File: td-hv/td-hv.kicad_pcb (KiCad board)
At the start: 2 copper layers, 100 x 60 mm, 39 parts, among them J1 Conn_01x06_Male, Q1 IMBF170R450M1XTMA1, U1 UCC2801, U2 TL081, U3 LM2903

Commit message: some td-hv layout
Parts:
- added C10: 0.1uF, Capacitor_SMD:C_0805_2012Metric, F.Cu at (-69.0, -17.0)
- added D4: BAS21, Package_TO_SOT_SMD:SOT-23, F.Cu at (-15.3, -29.9)
- added D5: SMAJ400ALFCT-ND, Diode_SMD:D_SMA, F.Cu at (-15.5, -24.5)
- added R14: 50, Resistor_SMD:R_1206_3216Metric, F.Cu at (-22.9, -30.4)
- J1: value Conn_01x06_Male -> Conn_01x07_Male; footprint Connector_JST:JST_XH_B6B-XH-AM_1x06_P2.50mm_Vertical -> Connector_JST:JST_XH_B7B-XH-AM_1x07_P2.50mm_Vertical
- R10, R4: footprint Resistor_SMD:R_0805_2012Metric -> Resistor_SMD:R_1206_3216Metric
- R11: value 100k -> 120
- R12: value 100 -> 50
- U2: value TL081 -> TLC272
- moved C4 60.3 mm to (-8.00, -15.0)
- moved C5 54.2 mm to (-7.05, -24.0), turned to 0 degrees
- moved R10 46.7 mm to (-23.0, -24.5), turned to 0 degrees
- moved C8 43.3 mm to (-61.0, -31.5), turned to 0 degrees
- moved R11 38.5 mm to (-77.0, -17.0)
- moved Q1 36.0 mm to (-45.0, -27.5)
- moved R4 35.8 mm to (-56.0, -24.0), turned to 270 degrees
- moved D1 35.5 mm to (-59.0, -12.5)
- moved R5 35.5 mm to (-59.0, -15.5)
- moved R3 35.2 mm to (-56.0, -31.0), turned to 180 degrees
- moved C7 34.7 mm to (-30.9, -24.5), turned to 0 degrees
- moved C6 34.5 mm to (-63.0, -11.5), turned to 270 degrees
- moved E1 33.3 mm to (-31.4, -31.0)
- moved R12 31.3 mm to (-73.0, -17.0), turned to 0 degrees
- moved C1 30.1 mm to (-71.0, -25.4)
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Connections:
- net Net-(C7-Pad2) renamed /snubber_node
- net Net-(F1-Pad2) renamed /vbus_in
- C3 pad 2: GND -> Net-(C3-Pad2)
- C8 pad 1: +12V -> Net-(C8-Pad1)
- R11 pad 1: Net-(L1-Pad7) -> Net-(C3-Pad2)
- R11 pad 2: GND -> /sync_in
- R12 pad 1: /eht_current -> Net-(C3-Pad2)
- R13 pad 2: Net-(R13-Pad2) -> Net-(C8-Pad1)
- R2 pad 2: GND -> /ucc3801_ref
- U1 pad 7: Net-(R13-Pad2) -> Net-(C8-Pad1)
- U2 pad 1: Net-(U2-Pad1) -> /eht_voltage
- U2 pad 5: Net-(U2-Pad5) -> (no net)
- U2 pad 6: /eht_voltage -> (no net)
- U2 pad 7: +12V -> (no net)
- U2 pad 8: Net-(U2-Pad8) -> +12V
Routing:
- net Net-(L1-Pad7): track 0.00 -> 57.2 mm
- net /eht_current: track 0.00 -> 54.5 mm, vias 0 -> 1
- net /fb: track 0.00 -> 53.4 mm
- net /eht_voltage: track 0.00 -> 49.0 mm, vias 0 -> 2
- net /sw: track 0.00 -> 33.2 mm
- net Net-(RV1-Pad2): track 0.00 -> 26.2 mm
- net VBUS: track 0.00 -> 24.8 mm
- net /sync_in: track 0.00 -> 24.6 mm
- net +12V: track 0.00 -> 24.2 mm, vias 0 -> 1
- net /cs: track 0.00 -> 22.5 mm
- net /~xray_protect: track 0.00 -> 16.8 mm, vias 0 -> 2
- net Net-(C6-Pad1): track 0.00 -> 16.3 mm
- net /ucc3801_ref: track 0.00 -> 13.6 mm, vias 0 -> 2
- net /vbus_in: track 0.00 -> 13.4 mm
- net Net-(D1-Pad1): track 0.00 -> 12.8 mm
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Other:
- board size 100 x 60 mm -> 90 x 66 mm
- net class hv added: clearance 1.5, trace_width 0.25, via_dia 0.8, via_drill 0.4
- board text added: "+12v"
- board text added: "b+"
- board text added: "eht_i"
- board text added: "eht_v"
- board text added: "gnd"
- board text added: "sync"
- board text added: "xray"
- board text removed: "Discharge Capacitors Before Servicing"

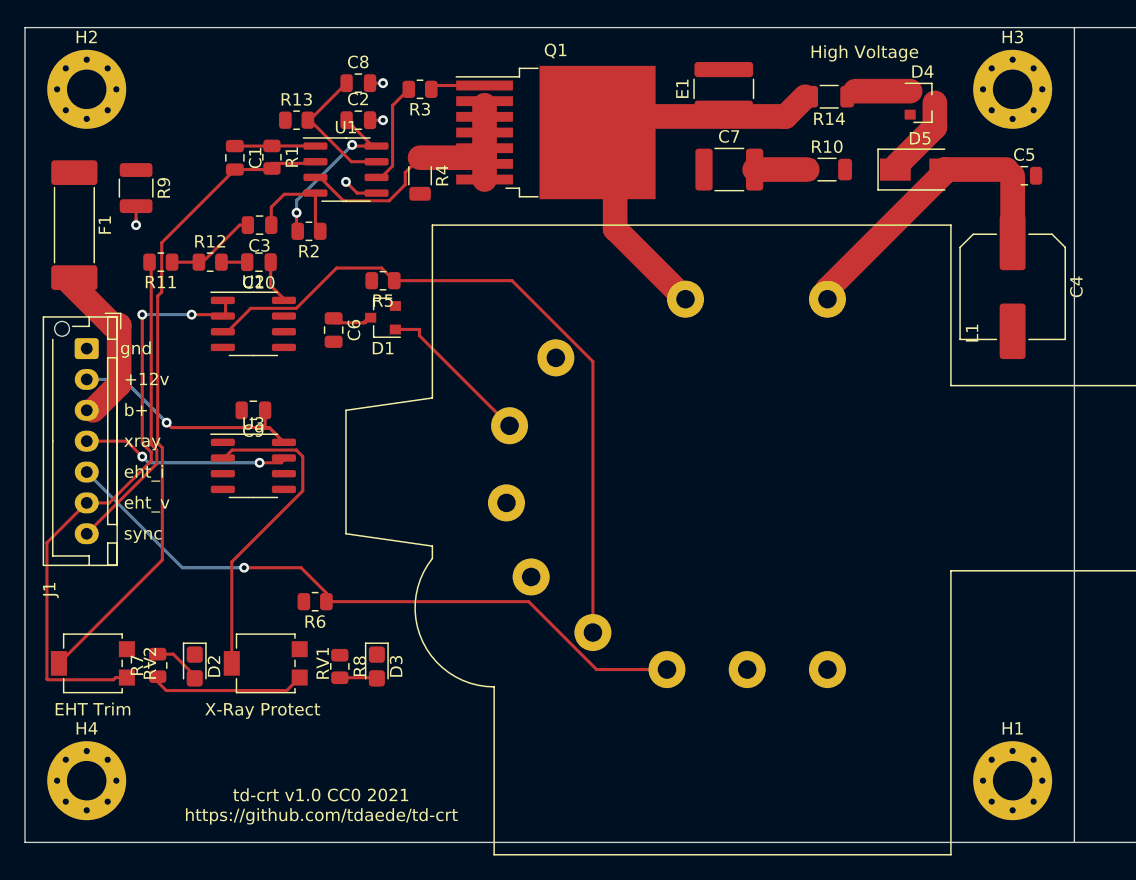
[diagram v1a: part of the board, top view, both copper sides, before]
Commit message: add output for vertical ssr
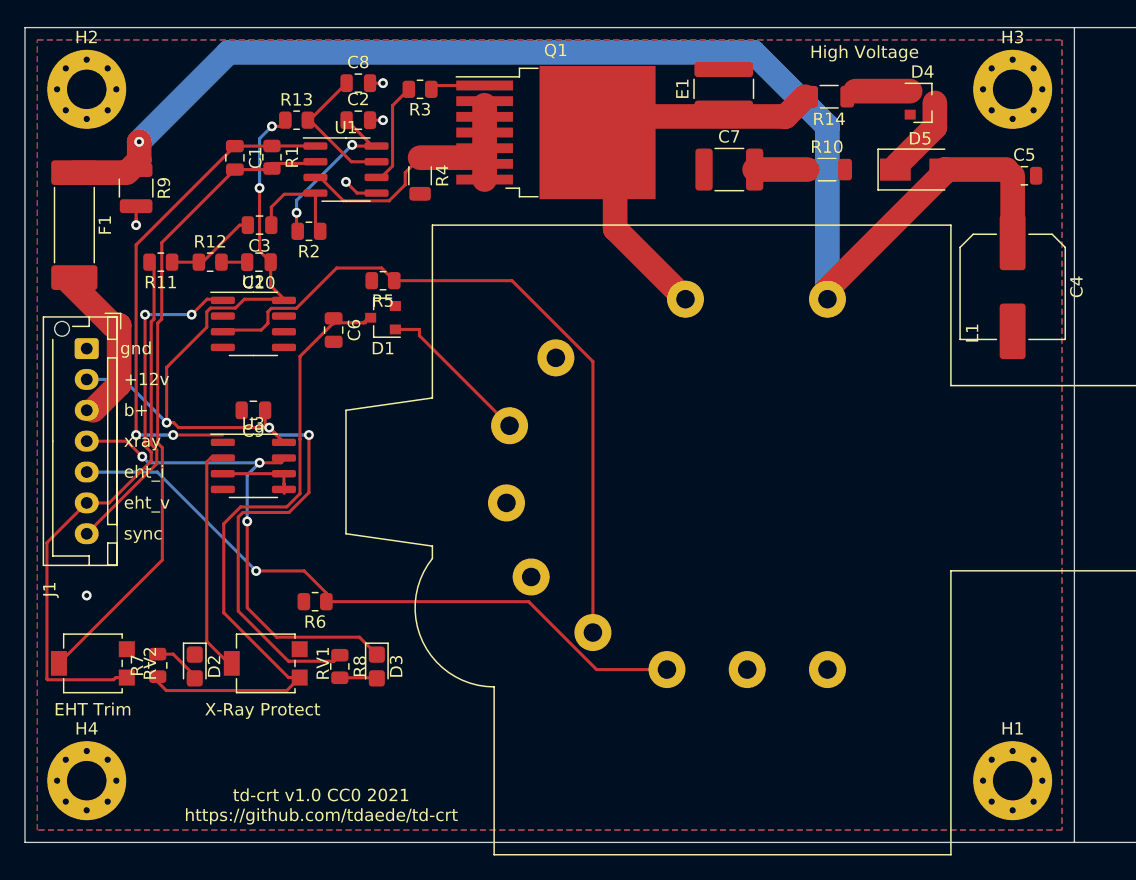
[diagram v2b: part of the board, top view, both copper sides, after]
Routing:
- net VBUS: track 24.8 -> 107.0 mm, vias 0 -> 1
- net +12V: track 24.2 -> 86.4 mm, vias 1 -> 5
- net Net-(C6-Pad1): track 16.3 -> 53.9 mm
- net /comp: track 5.49 -> 39.2 mm, vias 0 -> 2
- net /~xray_protect: track 16.8 -> 41.1 mm, vias 2 -> 3
- net Net-(RV1-Pad2): track 26.2 -> 18.7 mm
- net /ucc3801_ref: track 13.6 -> 20.3 mm
- net /eht_voltage: track 49.0 -> 47.9 mm
- net Net-(L1-Pad7): track 57.2 -> 57.7 mm
- net (no net): vias 0 -> 1
- added copper zone on B.Cu, net GND
- added copper zone on F.Cu, net GND

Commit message: stuff
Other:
- board size 90 x 66 mm -> 85 x 66 mm

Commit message: more td-hv layout
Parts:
- added REF**: KiCad-Logo_5mm_SilkScreen, Symbol:KiCad-Logo_5mm_SilkScreen, F.Cu at (-75.8, -33.2)
- added REF**: OSHW-Symbol_6.7x6mm_SilkScreen, Symbol:OSHW-Symbol_6.7x6mm_SilkScreen, F.Cu at (-7.80, 13.2)
- moved R5 17.8 mm to (-73.4, -5.00), turned to 0 degrees
- moved H2 7.07 mm to (-88.0, -36.0)
- moved H3 5.00 mm to (-8.00, -36.0)
- moved H4 5.00 mm to (-88.0, 25.0)
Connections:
- J1 pad 6: /eht_voltage -> /fb
- R5 pad 1: Net-(L1-Pad7) -> Net-(R5-Pad1)
- RV2 pad 1: /eht_voltage -> Net-(L1-Pad7)
- RV2 pad 2: /fb -> Net-(R5-Pad1)
- RV2 pad 3: GND -> Net-(R5-Pad1)
- U2 pad 1: /eht_voltage -> /fb
- U2 pad 2: /eht_voltage -> /fb
- U2 pad 3: Net-(L1-Pad7) -> Net-(R5-Pad1)
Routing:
- net /eht_voltage: track 47.9 -> 0.00 mm, vias 2 -> 0
- net Net-(R5-Pad1): track 0.00 -> 37.0 mm
- net /ucc3801_ref: track 20.3 -> 40.7 mm
- net /sw: track 33.2 -> 20.4 mm, vias 0 -> 13
- net Net-(L1-Pad7): track 57.7 -> 45.7 mm
- net VBUS: track 107.0 -> 115.4 mm
- net +12V: track 86.4 -> 79.8 mm
- net /fb: track 53.4 -> 54.5 mm
- net /sync_in: track 24.8 -> 24.1 mm
- net GND: vias 4 -> 41
- net (no net): vias 1 -> 0
- added copper zone on B.Cu, net /sw
- added copper zone on F.Cu, net /sw
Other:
- board size 85 x 66 mm -> 90 x 71 mm
- board text added: "td-hv v1.0 CERN OHL-W 2021 https://github.com/tdaede/td-crt"
- board text removed: "td-crt v1.0 CC0 2021 https://github.com/tdaede/td-crt"

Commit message: finish layout
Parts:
- removed REF**: KiCad-Logo_5mm_SilkScreen, Symbol:KiCad-Logo_5mm_SilkScreen
- removed REF**: OSHW-Symbol_6.7x6mm_SilkScreen, Symbol:OSHW-Symbol_6.7x6mm_SilkScreen
- added C11: 0.1uF, Capacitor_SMD:C_0805_2012Metric, F.Cu at (-65.5, -7.50)
- added C12: 0.001uF, Capacitor_SMD:C_0805_2012Metric, F.Cu at (-63.5, -12.5)
- added C13: 0.001uF, Capacitor_SMD:C_0805_2012Metric, F.Cu at (-47.5, -28.7)
- added C14: 0.1uF, Capacitor_SMD:C_0805_2012Metric, F.Cu at (-69.5, -7.50)
- added R16: 10k, Resistor_SMD:R_0805_2012Metric, F.Cu at (-58.9, -12.0)
- added R17: 10k, Resistor_SMD:R_0805_2012Metric, F.Cu at (-47.4, -31.5)
- added R18: 10, Resistor_SMD:R_0805_2012Metric, F.Cu at (-47.5, -34.0)
- added R19: 100k, Resistor_SMD:R_0805_2012Metric, F.Cu at (-69.5, -5.00)
- added R20: 100k, Resistor_SMD:R_0805_2012Metric, F.Cu at (-73.5, -7.50)
- added R21: 10k, Resistor_SMD:R_0805_2012Metric, F.Cu at (-76.9, -36.0)
- added R22: 100k, Resistor_SMD:R_0805_2012Metric, F.Cu at (-76.9, -32.5)
- C1: value 10000pF -> 0.1uF
- C3: value 22000pF -> 0.1uF
- C5: footprint Capacitor_SMD:C_0805_2012Metric -> Capacitor_SMD:C_1206_3216Metric
- C7: value 470pF 2000V NP0 -> 47pF 2000V NP0; footprint Capacitor_SMD:C_1812_4532Metric -> Capacitor_SMD:C_1206_3216Metric
- D2: value LED -> GREEN
- D3: value LED -> RED
- D4: value BAS21 -> GREEN; footprint Package_TO_SOT_SMD:SOT-23 -> LED_SMD:LED_0805_2012Metric
- D5: value SMAJ400ALFCT-ND -> GREEN; footprint Diode_SMD:D_SMA -> LED_SMD:LED_0805_2012Metric
- R10: value 20k -> 3k; footprint Resistor_SMD:R_1206_3216Metric -> Resistor_SMD:R_2512_6332Metric
- R11: value 120 -> 39k
- R12: value 50 -> 10k
- R13: value 1k -> 1.4k
- R14: value 50 -> 10k; footprint Resistor_SMD:R_1206_3216Metric -> Resistor_SMD:R_0805_2012Metric
- R2: value 10k -> 100k
- R3: value 1 -> 1M
- R4: value 1 -> 4.7
- U1: value UCC2801 -> UCC35701; footprint Package_SO:SOIC-8_3.9x4.9mm_P1.27mm -> Package_SO:SOIC-14_3.9x8.7mm_P1.27mm
- moved D5 57.6 mm to (-72.5, -32.5), turned to 180 degrees
- moved D4 57.5 mm to (-72.5, -36.0), turned to 180 degrees
- moved R14 45.5 mm to (-63.5, -10.0), turned to 0 degrees
- moved C5 34.6 mm to (-40.0, -34.5)
- moved C4 34.2 mm to (-40.0, -27.0)
- moved R4 23.5 mm to (-32.5, -22.0), turned to 180 degrees
- moved R10 21.1 mm to (-39.2, -38.0)
- moved R13 20.2 mm to (-47.5, -36.5), turned to 180 degrees
- moved Q1 18.8 mm to (-26.3, -29.5)
- moved E1 18.7 mm to (-13.5, -25.8), turned to 0 degrees
- moved C2 14.5 mm to (-47.5, -23.2)
- moved C7 13.1 mm to (-32.2, -37.5)
- moved C1 11.0 mm to (-60.0, -25.7), turned to 180 degrees
- moved U1 10.0 mm to (-53.8, -30.2), turned to 180 degrees
- moved R3 10.00 mm to (-47.5, -25.7), turned to 0 degrees
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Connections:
- net /~xray_protect renamed /~{xray_protect}
- C1 pad 1: /comp -> /ss
- C1 pad 2: /fb -> GND
- C2 pad 1: /ucc3801_ref -> Net-(C2-Pad1)
- C3 pad 1: Net-(C3-Pad1) -> GND
- C7 pad 1: /sw -> Net-(C7-Pad1)
- C7 pad 2: /snubber_node -> /sw
- C8 pad 1: Net-(C8-Pad1) -> +5V
- D1 pad 2: Net-(D1-Pad2) -> unconnected-(D1-Pad2)
- D1 pad 3: Net-(C6-Pad1) -> Net-(D1-Pad3)
- D4 pad 1: Net-(D4-Pad1) -> GND
- D5 pad 1: Net-(D4-Pad3) -> GND
- D5 pad 2: VBUS -> Net-(D5-Pad2)
- L1 pad 1: VBUS -> /sw
- L1 pad 2: /sw -> VBUS
- L1 pad 3: GND -> Net-(D1-Pad1)
- L1 pad 4: Net-(D1-Pad1) -> unconnected-(L1-Pad4)
- L1 pad 5: Net-(L1-Pad5) -> GND
- L1 pad 6: Net-(L1-Pad6) -> unconnected-(L1-Pad6)
- L1 pad 9: Net-(L1-Pad9) -> unconnected-(L1-Pad9)
- Q1 pad 2: /cs -> unconnected-(Q1-Pad2)
- Q1 pad 3: /cs -> Net-(Q1-Pad3)
- Q1 pad 4: /cs -> Net-(Q1-Pad3)
- Q1 pad 5: /cs -> Net-(Q1-Pad3)
- Q1 pad 6: /cs -> Net-(Q1-Pad3)
- Q1 pad 7: /cs -> Net-(Q1-Pad3)
- R1 pad 1: /comp -> +5V
- R1 pad 2: /fb -> Net-(R1-Pad2)
- R10 pad 1: /snubber_node -> VBUS
- R10 pad 2: GND -> Net-(C7-Pad1)
- R11 pad 1: Net-(C3-Pad2) -> +5V
- R11 pad 2: /sync_in -> Net-(R11-Pad2)
- R12 pad 1: Net-(C3-Pad2) -> Net-(R11-Pad2)
- R13 pad 1: +12V -> GND
- R13 pad 2: Net-(C8-Pad1) -> Net-(R13-Pad2)
- R14 pad 1: Net-(D4-Pad1) -> Net-(C11-Pad2)
- R14 pad 2: /sw -> Net-(C12-Pad2)
- R2 pad 1: Net-(C3-Pad1) -> Net-(R1-Pad2)
- R2 pad 2: /ucc3801_ref -> GND
- R3 pad 1: Net-(Q1-Pad1) -> Net-(C2-Pad1)
- R3 pad 2: Net-(R3-Pad2) -> GND
- R4 pad 1: /cs -> Net-(Q1-Pad3)
- R5 pad 1: Net-(R5-Pad1) -> Net-(L1-Pad7)
- R5 pad 2: GND -> Net-(C12-Pad2)
- RV2 pad 1: Net-(L1-Pad7) -> GND
- RV2 pad 2: Net-(R5-Pad1) -> Net-(RV2-Pad2)
- RV2 pad 3: Net-(R5-Pad1) -> +5V
- U1 pad 1: /comp -> Net-(C2-Pad1)
- U1 pad 2: /fb -> Net-(C13-Pad1)
- U1 pad 3: /cs -> +12V
- U1 pad 4: Net-(C3-Pad1) -> Net-(R18-Pad1)
- U1 pad 6: Net-(R3-Pad2) -> Net-(R11-Pad2)
- U1 pad 7: Net-(C8-Pad1) -> Net-(R13-Pad2)
- U1 pad 8: /ucc3801_ref -> /fb
- U2 pad 2: /fb -> Net-(C12-Pad2)
- U2 pad 3: Net-(R5-Pad1) -> Net-(RV2-Pad2)
- U3 pad 1: /comp -> /ss
- U3 pad 3: /ucc3801_ref -> +5V
- U3 pad 5: /ucc3801_ref -> +5V
- U3 pad 6: /ucc3801_ref -> Net-(RV1-Pad2)
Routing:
- net +5V: track 0.00 -> 81.7 mm, vias 0 -> 4
- net /ucc3801_ref: track 40.7 -> 0.00 mm, vias 2 -> 0
- net /ss: track 0.00 -> 39.6 mm, vias 0 -> 2
- net /comp: track 39.5 -> 0.00 mm, vias 2 -> 0
- net Net-(R5-Pad1): track 37.0 -> 0.00 mm
- net Net-(R11-Pad2): track 0.00 -> 35.3 mm
- net +12V: track 79.8 -> 114.2 mm, vias 5 -> 3
- net Net-(RV2-Pad2): track 0.00 -> 34.2 mm
- net VBUS: track 115.4 -> 88.4 mm, vias 1 -> 0
- net /sync_in: track 24.1 -> 51.0 mm
- net Net-(C12-Pad2): track 0.00 -> 26.5 mm
- net Net-(Q1-Pad3): track 0.00 -> 24.2 mm, vias 0 -> 2
- net Net-(R1-Pad2): track 0.00 -> 23.2 mm, vias 0 -> 2
- net /cs: track 22.5 -> 0.00 mm
- net /fb: track 54.5 -> 75.1 mm, vias 0 -> 2
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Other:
- net class Default removed
- net class hv removed
- board text added: "td-hv v1.1 CERN OHL-W 2021 https://github.com/tdaede/td-crt"
- board text removed: "td-hv v1.0 CERN OHL-W 2021 https://github.com/tdaede/td-crt"

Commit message: td-hv 2.0 changes
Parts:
- removed C10, C11, C14: 0.1uF, Capacitor_SMD:C_0805_2012Metric
- removed C12, C13: 0.001uF, Capacitor_SMD:C_0805_2012Metric
- removed D5: GREEN, LED_SMD:LED_0805_2012Metric
- removed E1: SPARK_GAP, Resistor_SMD:R_1218_3246Metric_Pad1.22x4.75mm_HandSolder
- removed R12, R14, R16, R17, R21: 10k, Resistor_SMD:R_0805_2012Metric
- removed R13: 1.4k, Resistor_SMD:R_0805_2012Metric
- removed R18: 10, Resistor_SMD:R_0805_2012Metric
- removed R19, R20, R22: 100k, Resistor_SMD:R_0805_2012Metric
- removed RV2: 1k, Potentiometer_SMD:Potentiometer_Bourns_3314G_Vertical
- removed U3: LM2903, Package_SO:SOIC-8_3.9x4.9mm_P1.27mm
- added C19: 0.1uF, Capacitor_SMD:C_0805_2012Metric, F.Cu at (112.0, 90.0)
- added C24: 4700pF 2000V, Capacitor_THT:C_Rect_L18.0mm_W5.0mm_P15.00mm_FKS3_FKP3, F.Cu at (166.0, 84.5)
- added Q12: G3R450MT17J, td-hv:TO-263-7_TabPin8_GeneSiC, F.Cu at (152.9, 76.8)
- added Q2: BSZ42DN25NS3GATMA1, Package_TO_SOT_SMD:TDSON-8-1, F.Cu at (128.1, 80.2)
- added R105: 22k, Resistor_SMD:R_0805_2012Metric, F.Cu at (118.5, 92.4)
- added R106: 1k, Resistor_SMD:R_0805_2012Metric, F.Cu at (118.5, 96.5)
- added R33: 10k, Resistor_SMD:R_0805_2012Metric, F.Cu at (118.5, 100.6)
- added R34: 10k, Resistor_SMD:R_0805_2012Metric, F.Cu at (137.1, 70.2)
- added R35: 1, Resistor_SMD:R_0805_2012Metric, F.Cu at (140.9, 73.0)
- added R36: 0.01, Resistor_SMD:R_0805_2012Metric, F.Cu at (140.9, 78.0)
- added R41: 1M 3000V, Resistor_SMD:R_2512_6332Metric, F.Cu at (172.0, 88.0)
- added R42: 1k, Resistor_SMD:R_0805_2012Metric, F.Cu at (172.0, 94.1)
- added TP10: TestPoint, TestPoint:TestPoint_Keystone_5019_Minature, F.Cu at (112.2, 118.0)
- added TP4: TestPoint, TestPoint:TestPoint_Keystone_5019_Minature, F.Cu at (175.0, 94.5)
- added TP6: TestPoint, TestPoint:TestPoint_Keystone_5019_Minature, F.Cu at (91.5, 119.0)
- added TP7: TestPoint, TestPoint:TestPoint_Keystone_5019_Minature, F.Cu at (91.5, 123.5)
- added TP8: TestPoint, TestPoint:TestPoint_Keystone_5019_Minature, F.Cu at (123.0, 100.0)
- added TP9: TestPoint, TestPoint:TestPoint_Keystone_5019_Minature, F.Cu at (119.5, 87.0)
- added U13: MCP1416, Package_TO_SOT_SMD:SOT-23-5, F.Cu at (136.9, 74.0)
- added U4: 2ED2101S06FXUMA1, Package_SO:SOIC-8_3.9x4.9mm_P1.27mm, F.Cu at (117.0, 77.0)
- added U7: MIC5504-3.3YM5, Package_TO_SOT_SMD:SOT-23-5, F.Cu at (108.9, 106.0)
- C2: value 0.1uF -> 15uF 250V; footprint Capacitor_SMD:C_0805_2012Metric -> Capacitor_SMD:CP_Elec_10x10.5
- C4: value 12uF 250V -> 0.1uF; footprint Capacitor_SMD:C_Elec_8x10.2 -> Capacitor_SMD:C_0805_2012Metric
- C5: value 0.1uF 200V -> 47pF 2000V NP0; footprint Capacitor_SMD:C_1206_3216Metric -> Capacitor_SMD:C_1812_4532Metric
- C6: value 0.1uF -> 0.01uF
- C7: value 47pF 2000V NP0 -> 0.1uF; footprint Capacitor_SMD:C_1206_3216Metric -> Capacitor_SMD:C_0805_2012Metric
- C8: value 0.1uF -> 0.1uF 250V; footprint Capacitor_SMD:C_0805_2012Metric -> Capacitor_SMD:C_1206_3216Metric
- C9: value 0.1uF -> 1uF
- D1: value BAV99 -> RED; footprint Package_TO_SOT_SMD:SOT-23 -> LED_SMD:LED_0805_2012Metric
- D2: value GREEN -> ES1G-13-F; footprint LED_SMD:LED_0805_2012Metric_Castellated -> Diode_THT:D_DO-41_SOD81_P10.16mm_Horizontal
- D3: value RED -> BAT54A; footprint LED_SMD:LED_0805_2012Metric_Castellated -> Package_TO_SOT_SMD:SOT-23
- D4: value GREEN -> BAT54A; footprint LED_SMD:LED_0805_2012Metric -> Package_TO_SOT_SMD:SOT-23
- F1: value Fuse -> 400mA; footprint Fuse:Fuse_Schurter_UMT250 -> Fuse:Fuse_Schurter_UMZ250
- J1: value Conn_01x07_Male -> Conn_01x14; footprint Connector_JST:JST_XH_B7B-XH-AM_1x07_P2.50mm_Vertical -> Connector_JST:JST_XH_B14B-XH-A_1x14_P2.50mm_Vertical
- Q1: value IMBF170R450M1XTMA1 -> BSZ42DN25NS3GATMA1; footprint Package_TO_SOT_SMD:TO-263-7_TabPin8 -> Package_TO_SOT_SMD:TDSON-8-1
- R1, R8: value 10k -> 1k
- R10: value 3k -> 10k; footprint Resistor_SMD:R_2512_6332Metric -> Resistor_SMD:R_0805_2012Metric
- R11: value 39k -> 10k
- R2: value 100k -> 1k
- R3: value 1M -> 1
- R4: value 4.7 -> 1; footprint Resistor_SMD:R_1206_3216Metric -> Resistor_SMD:R_0805_2012Metric
- R5: value 100k -> 10k
- R6: value 100 -> 3k; footprint Resistor_SMD:R_0805_2012Metric -> Resistor_SMD:R_2512_6332Metric
- R7: value 10k -> 47k
- R9: value 100k -> 1k; footprint Resistor_SMD:R_1210_3225Metric -> Resistor_SMD:R_0805_2012Metric
- RV1: value 1k -> 10k
- U1: value UCC35701 -> 74HC00
- U2: value TLC272 -> LM2903
- moved R9 237.6 mm to (117.0, 111.3)
- moved D4 235.1 mm to (122.0, 96.1), turned to -90 degrees
- moved R5 230.5 mm to (118.0, 123.4), turned to 90 degrees
- moved C6 230.4 mm to (124.8, 130.1), turned to -90 degrees
- moved R6 227.3 mm to (150.0, 85.5)
- moved R8 221.8 mm to (127.5, 130.1)
- moved R1 221.2 mm to (104.3, 127.5), turned to 0 degrees
- moved U2 220.4 mm to (112.0, 113.1)
- moved R2 219.8 mm to (115.5, 105.9), turned to 90 degrees
- moved D1 218.6 mm to (104.3, 129.8), turned to 0 degrees
- moved C5 218.4 mm to (142.5, 85.5), turned to 180 degrees
- moved R11 216.3 mm to (114.2, 84.1), turned to -90 degrees
- moved C8 214.1 mm to (130.5, 68.5), turned to 0 degrees
- moved R7 211.9 mm to (107.0, 120.4)
- moved C3 211.6 mm to (122.0, 71.0), turned to 0 degrees
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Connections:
- net /vbus_in renamed Net-(J1-Pin_3)
- C1 pad 1: /ss -> +12V
- C2 pad 1: Net-(C2-Pad1) -> HT
- C3 pad 1: GND -> Net-(D2-K)
- C3 pad 2: Net-(C3-Pad2) -> Net-(Q2-D)
- C4 pad 1: VBUS -> Net-(U2A--)
- C5 pad 1: VBUS -> /flyback/snub
- C5 pad 2: GND -> Net-(Q2-D)
- C6 pad 1: Net-(C6-Pad1) -> BEAM_CURRENT
- C7 pad 2: /sw -> GND
- C8 pad 1: +5V -> HT
- C9 pad 1: +12V -> +3.3V
- D1 pad 1: Net-(D1-Pad1) -> HV_PROTECT
- D1 pad 2: unconnected-(D1-Pad2) -> Net-(D1-A)
- D2 pad 1: GND -> Net-(D2-K)
- D2 pad 2: Net-(D2-Pad2) -> +12V
- D3 pad 1: /~{xray_protect} -> Net-(U2A--)
- D3 pad 2: Net-(D3-Pad2) -> unconnected-(D3-Pad2)
- D4 pad 1: GND -> unconnected-(D4-Pad1)
- D4 pad 2: Net-(D4-Pad2) -> Net-(C7-Pad1)
- F1 pad 1: VBUS -> HT
- J1 pad 1: GND -> +12V
- J1 pad 2: +12V -> GND
- J1 pad 4: /~{xray_protect} -> GND
- J1 pad 5: /eht_current -> EHT_PWM
- J1 pad 6: /fb -> HV_HI
- J1 pad 7: /sync_in -> HV_LO
- L1 pad 1: /sw -> /flyback/eht out
- L1 pad 2: VBUS -> Net-(Q2-D)
- L1 pad 3: Net-(D1-Pad1) -> GND
- L1 pad 4: unconnected-(L1-Pad4) -> Net-(D4-Pad3)
- L1 pad 5: GND -> Net-(D3-Pad3)
- L1 pad 7: Net-(L1-Pad7) -> EHT_VOLTAGE_DIVIDER
- L1 pad 8: /eht_current -> BEAM_CURRENT
- Q1 pad 1: Net-(Q1-Pad1) -> Net-(Q2-D)
- Q1 pad 2: unconnected-(Q1-Pad2) -> Net-(Q2-D)
- Q1 pad 3: Net-(Q1-Pad3) -> Net-(Q2-D)
- Q1 pad 4: Net-(Q1-Pad3) -> Net-(Q1-G)
- Q1 pad 5: Net-(Q1-Pad3) -> HT
- R1 pad 1: +5V -> +3.3V
- R1 pad 2: Net-(R1-Pad2) -> Net-(D1-A)
- R10 pad 1: VBUS -> HV_HI
- R10 pad 2: Net-(C7-Pad1) -> GND
- R11 pad 1: +5V -> HV_LO
- R11 pad 2: Net-(R11-Pad2) -> GND
- R2 pad 1: Net-(R1-Pad2) -> +3.3V
- R2 pad 2: GND -> Net-(R2-Pad2)
- R3 pad 1: Net-(C2-Pad1) -> Net-(Q1-G)
- R3 pad 2: GND -> Net-(U4-HO)
- R4 pad 1: Net-(Q1-Pad3) -> Net-(Q2-G)
- R4 pad 2: GND -> Net-(U4-LO)
- R5 pad 1: Net-(L1-Pad7) -> +12V
- R5 pad 2: Net-(C12-Pad2) -> Net-(R5-Pad2)
- R6 pad 1: /eht_current -> /flyback/eht out
- R6 pad 2: GND -> /flyback/snub
- R7 pad 1: Net-(C6-Pad1) -> EHT_VOLTAGE_DIVIDER
- R7 pad 2: Net-(D2-Pad2) -> GND
- R8 pad 1: +12V -> BEAM_CURRENT
- R8 pad 2: Net-(D3-Pad2) -> GND
- R9 pad 1: VBUS -> +3.3V
- R9 pad 2: GND -> HV_PROTECT
- RV1 pad 1: Net-(C6-Pad1) -> GND
- RV1 pad 2: Net-(RV1-Pad2) -> Net-(U2A-+)
- RV1 pad 3: GND -> Net-(R5-Pad2)
- U1 pad 1: Net-(C2-Pad1) -> Net-(R2-Pad2)
- U1 pad 10: Net-(C3-Pad2) -> GND
- U1 pad 11: /sync_in -> unconnected-(U1-Pad11)
- U1 pad 12: +5V -> GND
- U1 pad 14: /ss -> +3.3V
- U1 pad 2: Net-(C13-Pad1) -> EHT_PWM
- U1 pad 3: +12V -> Net-(U1-Pad3)
- U1 pad 4: Net-(R18-Pad1) -> Net-(U1-Pad3)
- U1 pad 5: GND -> Net-(U1-Pad3)
- U1 pad 6: Net-(R11-Pad2) -> Net-(U13-IN)
- U1 pad 7: Net-(R13-Pad2) -> GND
- U1 pad 8: /fb -> unconnected-(U1-Pad8)
- U1 pad 9: Net-(R1-Pad2) -> GND
- U2 pad 1: /fb -> Net-(R2-Pad2)
- U2 pad 2: Net-(C12-Pad2) -> Net-(U2A--)
- U2 pad 3: Net-(RV2-Pad2) -> Net-(U2A-+)
- U2 pad 5: (no net) -> Net-(U2A--)
- U2 pad 6: (no net) -> Net-(U2A-+)
- U2 pad 7: (no net) -> HV_PROTECT
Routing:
- net EHT_FLYBACK_VOLTAGE: track 0.00 -> 135.4 mm, vias 0 -> 2
- net EHT_FLYBACK_CURRENT: track 0.00 -> 103.6 mm, vias 0 -> 2
- net VBUS: track 88.4 -> 0.00 mm
- net +5V: track 81.7 -> 0.00 mm, vias 4 -> 0
- net /fb: track 75.1 -> 0.00 mm, vias 2 -> 0
- net BEAM_CURRENT: track 0.00 -> 66.2 mm, vias 0 -> 1
- net EHT_VOLTAGE_DIVIDER: track 0.00 -> 55.0 mm, vias 0 -> 2
- net /eht_current: track 54.6 -> 0.00 mm, vias 1 -> 0
- net Net-(Q2-D): track 0.00 -> 53.7 mm, vias 0 -> 3
- net /sync_in: track 51.0 -> 0.00 mm
- net Net-(C6-Pad1): track 45.6 -> 0.00 mm, vias 2 -> 0
- net HV_LO: track 0.00 -> 42.0 mm, vias 0 -> 2
- net HT: track 0.00 -> 41.3 mm
- net Net-(L1-Pad7): track 41.1 -> 0.00 mm
- net HV_HI: track 0.00 -> 40.8 mm, vias 0 -> 2
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- added copper zone on B.Cu, net /flyback/eht out
- added copper zone on F.Cu, net /flyback/eht out
- removed copper zone on B.Cu, net /sw
- removed copper zone on F.Cu, net /sw
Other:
- board text added: "beam_i"
- board text added: "div_v"
- board text added: "eht_t"
- board text added: "fb_i"
- board text added: "fb_v"
- board text added: "hot"
- board text added: "hv_hi"
- board text added: "hv_lo"
- board text added: "hv_prot"
- board text added: "td-hv v2.0 CERN OHL-W 2023 https://github.com/tdaede/td-crt"
- board text removed: "EHT Trim"
- board text removed: "eht_i"
- board text removed: "eht_v"
- board text removed: "sync"
- board text removed: "td-hv v1.1 CERN OHL-W 2021 https://github.com/tdaede/td-crt"
- board text removed: "xray"
